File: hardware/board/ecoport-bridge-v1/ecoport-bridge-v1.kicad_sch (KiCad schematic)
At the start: 64 parts, among them J1 420B2V12FL0, J2 Conn_01x02, J3 BM04B-SRSS-TB, J4 USB4085-GF-A, J5 Conn_01x02, J6 Connector Wire, J7 B3B-PH-K-S, SW1 RESET, SW2 BOOT, U1 IRM-05-5, U2 TLV75733PDBVR, U3 SP3485EET, U4 USBLC6-2SC6, U5 SN74LV1T34DCKR, U6 ESP32-C6-WROOM-1-N8, U7 USBLC6-2SC6, U8 LM66100DCKR

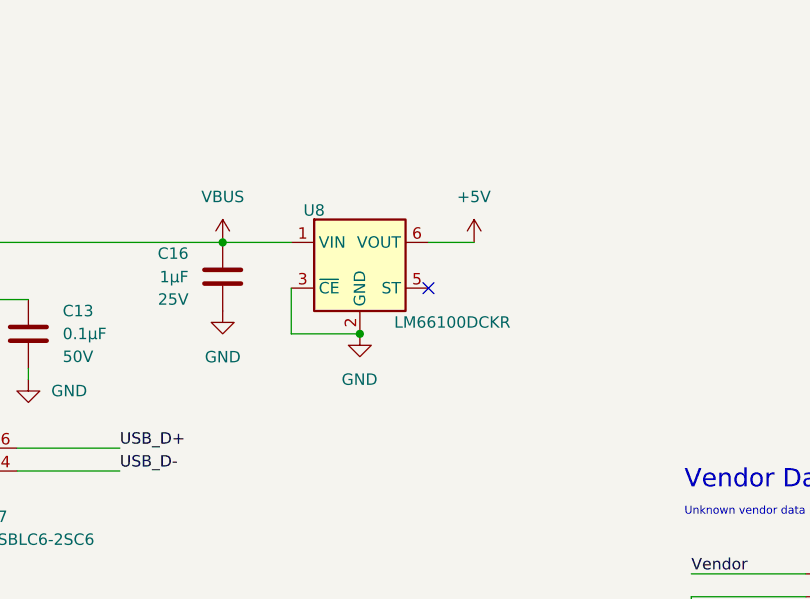
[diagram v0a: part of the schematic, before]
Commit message: Rounded traces, board edge, fixed diode traces
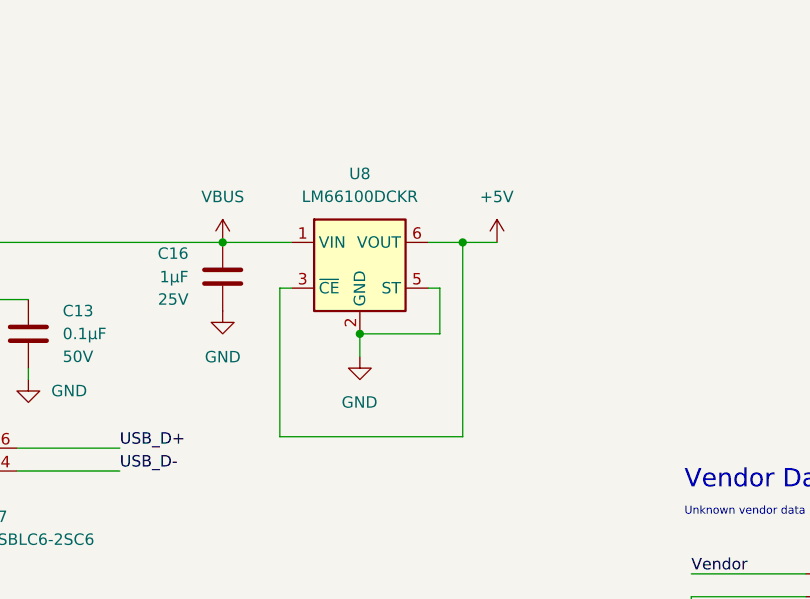
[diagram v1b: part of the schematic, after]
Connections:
- net +5V: now also U8.3 (~{CE})
- net GND: now also U8.5 (ST); no longer U8.3 (~{CE})
- no-connect marks 15 -> 14
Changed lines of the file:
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@@
 	)
 	(junction
-		(at 134.62 212.09)
-		(diameter 0)
-		(color 0 0 0 0)
-	)
-	(junction
 		(at 72.39 144.78)
 		(diameter 0)
@@
 	)
 	(junction
+		(at 134.62 212.09)
+		(diameter 0)
+		(color 0 0 0 0)
+	)
+	(junction
 		(at 370.84 191.77)
 		(diameter 0)
@@
 	)
 	(junction
+		(at 146.05 201.93)
+		(diameter 0)
+		(color 0 0 0 0)
+	)
+	(junction
 		(at 289.56 62.23)
 		(diameter 0)
@@
 	)
 	(no_connect
-		(at 142.24 207.01)
-	)
-	(no_connect
 		(at 60.96 236.22)
 	)
@@
 	(wire
 		(pts
-			(xy 142.24 201.93) (xy 147.32 201.93)
+			(xy 142.24 201.93) (xy 149.86 201.93)
 		)
 		(stroke
@@
 	(wire
 		(pts
+			(xy 125.73 207.01) (xy 125.73 223.52)
+		)
+		(stroke
+			(width 0)
+			(type default)
+		)
+	)
+	(wire
+		(pts
 			(xy 241.3 243.84) (xy 243.84 243.84)
 		)
@@
 	(wire
 		(pts
+			(xy 143.51 212.09) (xy 134.62 212.09)
+		)
+		(stroke
+			(width 0)
+			(type default)
+		)
+	)
+	(wire
+		(pts
 			(xy 60.96 226.06) (xy 62.23 226.06)
 		)
@@
 	(wire
 		(pts
+			(xy 134.62 214.63) (xy 134.62 212.09)
+		)
+		(stroke
+			(width 0)
+			(type default)
+		)
+	)
+	(wire
+		(pts
 			(xy 370.84 181.61) (xy 370.84 184.15)
 		)
@@
 	(wire
 		(pts
-			(xy 127 212.09) (xy 134.62 212.09)
-		)
-		(stroke
-			(width 0)
-			(type default)
-		)
-	)
-	(wire
-		(pts
 			(xy 370.84 123.19) (xy 370.84 140.97)
 		)
@@
 	(wire
 		(pts
-			(xy 127 207.01) (xy 127 212.09)
-		)
-		(stroke
-			(width 0)
-			(type default)
-		)
-	)
-	(wire
-		(pts
 			(xy 153.67 48.26) (xy 153.67 58.42)
 		)
@@
 	(wire
 		(pts
+			(xy 142.24 207.01) (xy 143.51 207.01)
+		)
+		(stroke
+			(width 0)
+			(type default)
+		)
+	)
+	(wire
+		(pts
 			(xy 336.55 58.42) (xy 336.55 59.69)
 		)
@@
 	(wire
 		(pts
+			(xy 125.73 207.01) (xy 127 207.01)
+		)
+		(stroke
+			(width 0)
+			(type default)
+		)
+	)
+	(wire
+		(pts
 			(xy 370.84 189.23) (xy 370.84 191.77)
 		)
@@
 	(wire
 		(pts
+			(xy 146.05 223.52) (xy 146.05 201.93)
+		)
+		(stroke
+			(width 0)
+			(type default)
+		)
+	)
+	(wire
+		(pts
 			(xy 285.75 72.39) (xy 285.75 64.77)
 		)
@@
 	(wire
 		(pts
+			(xy 143.51 207.01) (xy 143.51 212.09)
+		)
+		(stroke
+			(width 0)
+			(type default)
+		)
+	)
+	(wire
+		(pts
 			(xy 67.31 154.94) (xy 72.39 154.94)
 		)
@@
 	(wire
 		(pts
+			(xy 125.73 223.52) (xy 146.05 223.52)
+		)
+		(stroke
+			(width 0)
+			(type default)
+		)
+	)
+	(wire
+		(pts
 			(xy 284.48 146.05) (xy 289.56 146.05)
 		)
@@
 		(in_pos_files yes)
 		(dnp no)
+		(fields_autoplaced yes)
 		(property "Reference" "U8"
-			(at 129.54 198.374 0)
+			(at 134.62 194.31 0)
 			(show_name no)
 			(do_not_autoplace no)
@@
 		)
 		(property "Value" "LM66100DCKR"
-			(at 138.43 210.82 0)
+			(at 134.62 196.85 0)
 			(show_name no)
 			(do_not_autoplace no)
@@
 					(size 1.27 1.27)
 				)
-				(justify left)
 			)
 		)
@@
 	(symbol
 		(lib_id "power:+5V")
-		(at 147.32 201.93 0)
+		(at 149.86 201.93 0)
 		(unit 1)
 		(body_style 1)
@@
 		(fields_autoplaced yes)
 		(property "Reference" "#PWR047"
-			(at 147.29 205.77 0)
+			(at 149.83 205.77 0)
 			(hide yes)
 			(show_name no)
@@
 		)
 		(property "Value" "+5V"
-			(at 147.29 196.87 0)
+			(at 149.83 196.87 0)
 			(show_name no)
 			(do_not_autoplace no)
@@
 		)
 		(property "Footprint" ""
-			(at 147.29 201.97 0)
+			(at 149.83 201.97 0)
 			(hide yes)
 			(show_name no)
@@
 		)
 		(property "Datasheet" ""
-			(at 147.29 201.97 0)
+			(at 149.83 201.97 0)
 			(hide yes)
 			(show_name no)
@@
 		)
 		(property "Description" "Power symbol creates a global label with name \"+5V\""
-			(at 147.29 201.97 0)
+			(at 149.83 201.97 0)
 			(hide yes)
 			(show_name no)
@@
 	(symbol
 		(lib_id "power:GND")
-		(at 134.62 212.09 0)
+		(at 134.62 214.63 0)
 		(unit 1)
 		(body_style 1)
@@
 		(fields_autoplaced yes)
 		(property "Reference" "#PWR046"
-			(at 134.59 218.47 0)
+			(at 134.59 221.01 0)
 			(hide yes)
 			(show_name no)
@@
 		)
 		(property "Value" "GND"
-			(at 134.59 217.17 0)
+			(at 134.59 219.71 0)
 			(show_name no)
 			(do_not_autoplace no)
@@
 		)
 		(property "Footprint" ""
-			(at 134.59 212.07 0)
+			(at 134.59 214.61 0)
 			(hide yes)
 			(show_name no)
@@
 		)
 		(property "Datasheet" ""
-			(at 134.59 212.07 0)
+			(at 134.59 214.61 0)
 			(hide yes)
 			(show_name no)
@@
 		)
 		(property "Description" "Power symbol creates a global label with name \"GND\" , ground"
-			(at 134.59 212.07 0)
+			(at 134.59 214.61 0)
 			(hide yes)
 			(show_name no)

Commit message: cleanup
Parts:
- F1: symbol Custom:SF-2410SP050W-2 -> Custom:SF-2410SP100W-2
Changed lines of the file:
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@@
 	)
 	(symbol
-		(lib_id "Custom:SF-2410SP050W-2")
+		(lib_id "Custom:SF-2410SP100W-2")
 		(at 67.31 69.85 0)
 		(unit 1)
